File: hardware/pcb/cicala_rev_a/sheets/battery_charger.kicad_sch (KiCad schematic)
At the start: 35 parts, among them J1 USB-C receptacle, J3 Protected LiPo + NTC, U2 BQ25185DLH, U3 TPS63802DLA, U4 USBLC6-2SC6, U5 TPS22917DBVR

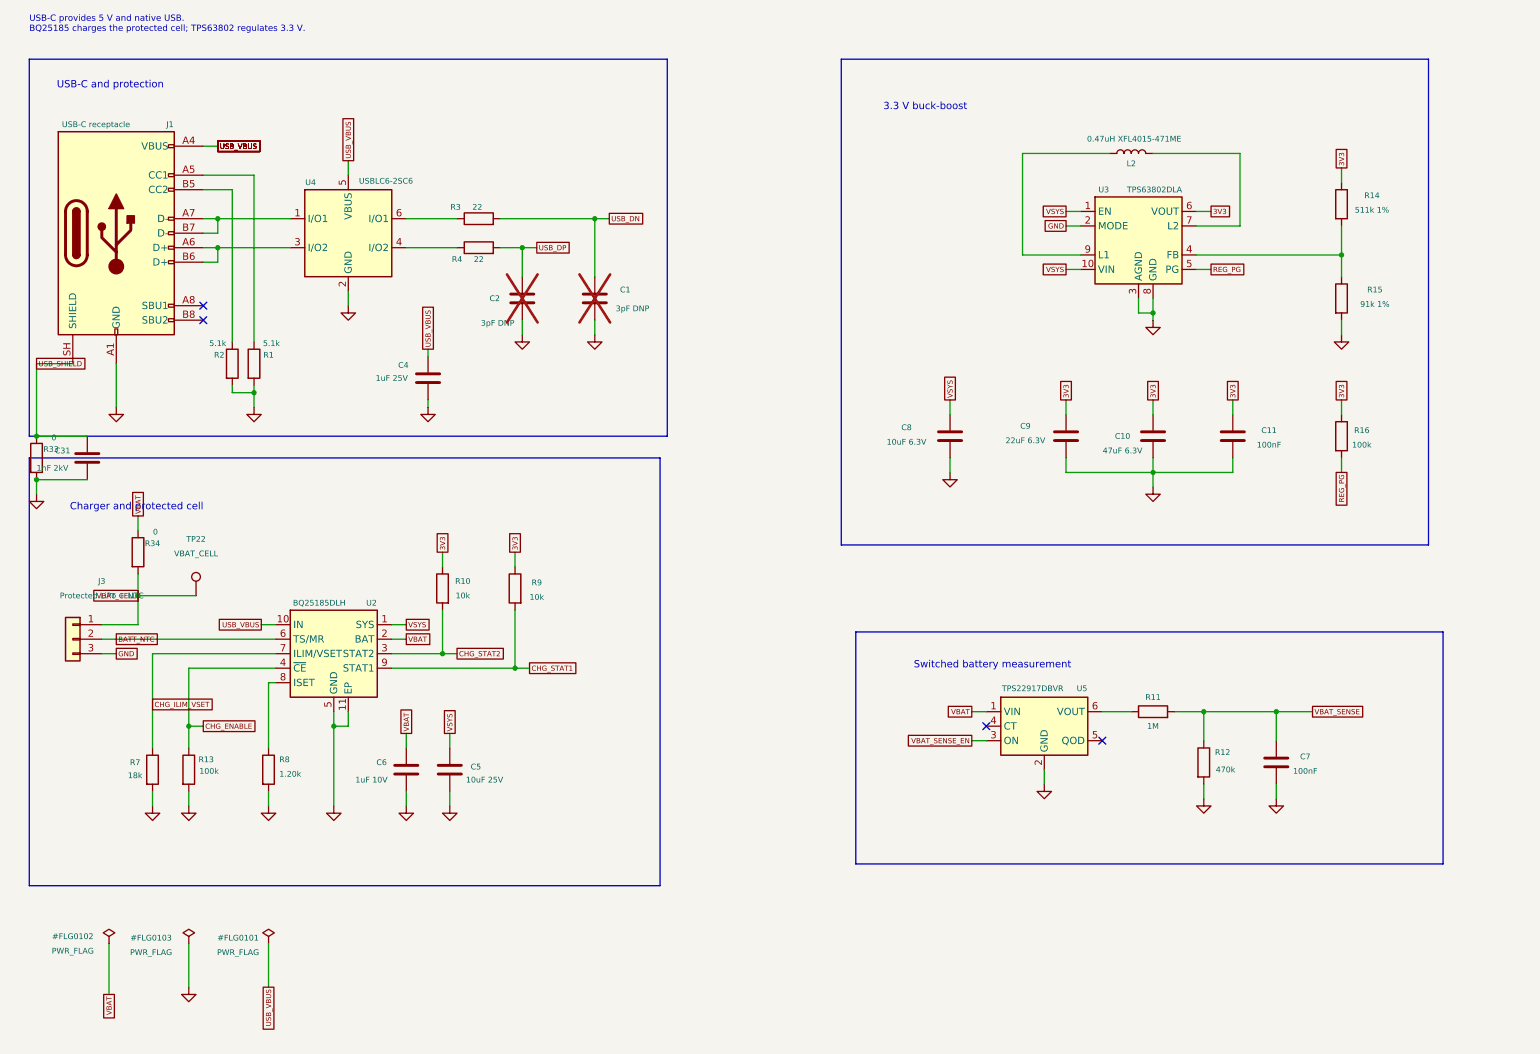
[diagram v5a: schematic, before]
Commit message: refactor(hw): make the root sheet a real hierarchy
The root was three boxes and a filename; every cross-sheet signal travelled
by global label, so nothing recorded which block produced a signal and which
consumed it. The 19 nets that actually cross a sheet boundary are now
hierarchical: each child carries a directional hierarchical label and the
root carries the matching sheet pin, wired block to block. The root also
states the power flow in words.

GND stays global; a ground symbol reads better than a pin on every block.
Root-level global labels keep the plain net names that pin_contract.csv and
the firmware refer to, rather than the sheet-path names a local label gives.

Connectivity is unchanged: the exported netlist is identical to the one
before the conversion, net for net and pin for pin.

Also hides the PWR_FLAG references, moves the USB shield network and the
cell-current link inside the blocks they belong to, and gives every page the
same company, revision and date.

Co-Authored-By: Claude Opus 5 <noreply@anthropic.com>
Claude-Session: https://claude.ai/code/session_01E5vy1HJsPztSk9nFw6j5Ko
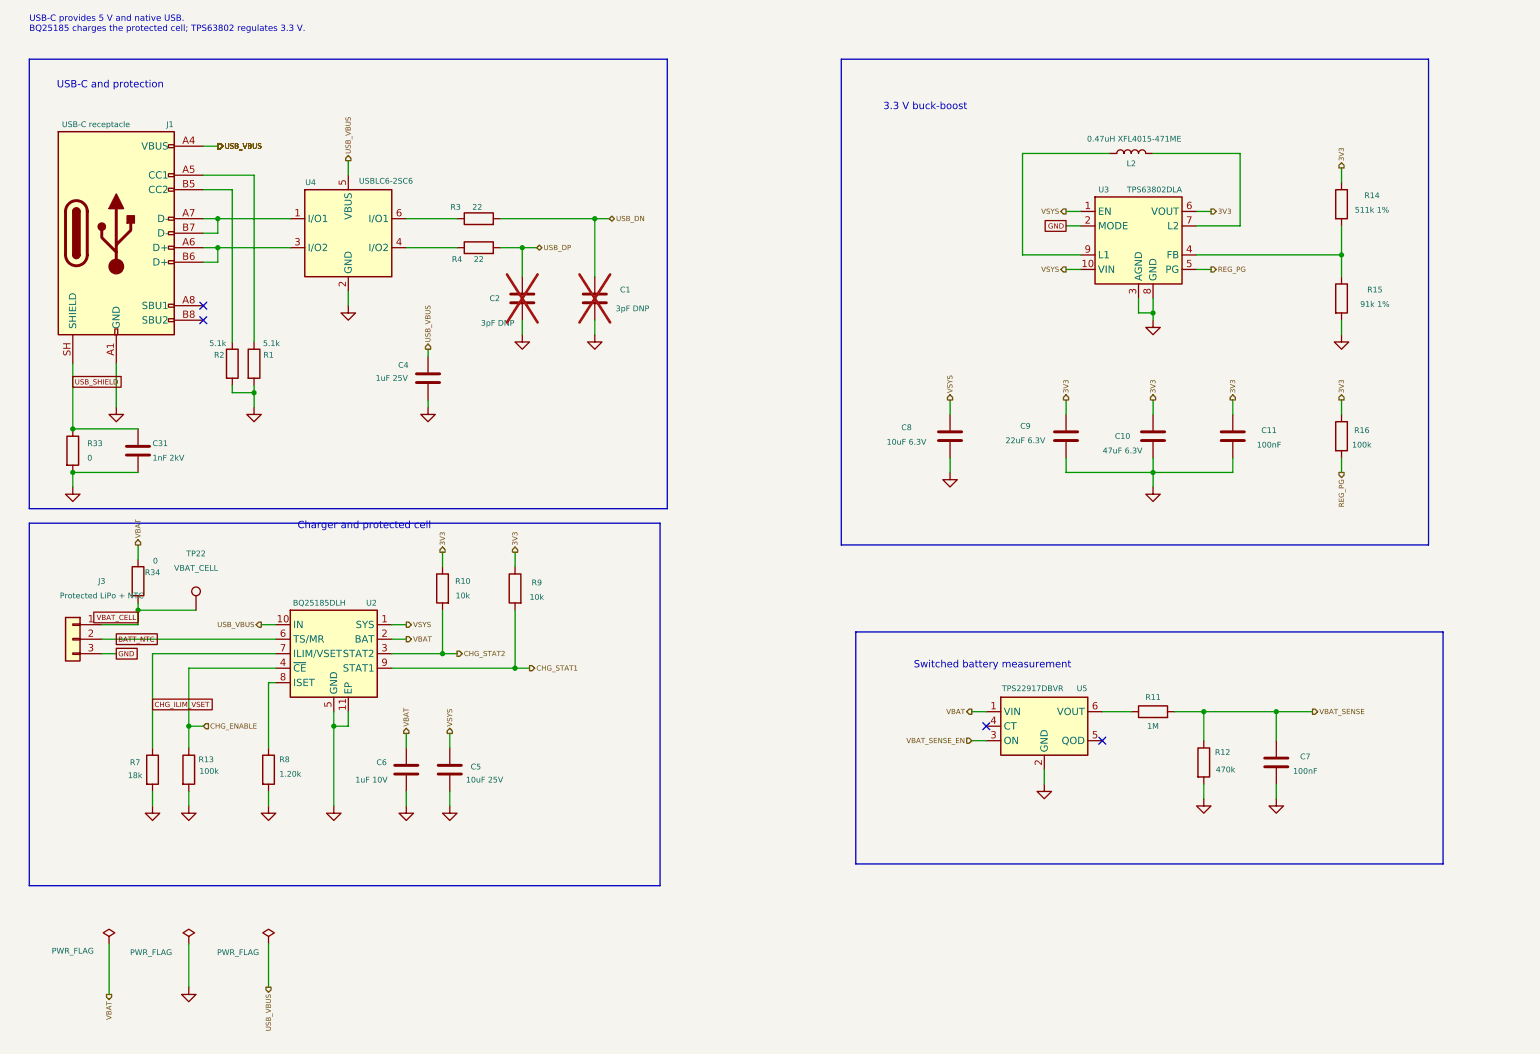
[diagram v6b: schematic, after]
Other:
- company: (none) -> Cicala
- moved on the sheet: C31, R33, R34, TP22

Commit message: feat(hw): place the Rev A board
Everything except the two switches and the display stack sits on the
underside, in the cell cavity, because the sloped roof leaves 0.8 to 3.5 mm
above the board. The module goes rear-left with its antenna at the board
edge and clear of the display; the cell keep-out, the power block and the
front connector row follow from that.

Placement is generated rather than dragged, so it can be regenerated after a
schematic change: anchors are chosen by hand, the rest are packed into free
regions ordered by distance to the pads they already share a net with.

Board is 78 x 49 mm at (3, 3.5). It grew 4 mm deeper than the old 78 x 45
because a USB-C plug could never have reached a receptacle sitting 6 mm
behind the case wall; the front edge now ends 1.5 mm from it and the
receptacle noses into the wall aperture.

Mounting holes become NPTH footprints instead of circles on Edge.Cuts, so
they are drilled rather than routed, and they move to x=13 to clear
Espressif's antenna keep-out, which the module footprint carries and which
reaches 9.5 mm in from the left edge.

J1 gets a project footprint whose silkscreen stops at the board edge; the
library outline would print past it, because the part deliberately overhangs.

Netclasses: Power 0.4 mm, USB 0.29 mm at a 0.29 mm gap for 90 ohm
differential over the declared 0.18 mm prepreg, HV 0.2 mm, which is the gap
the panel's own 0.5 mm-pitch connector allows.

DRC reports zero violations and zero schematic-parity issues. The 216
unconnected items are the routing, which is the next commit.

Co-Authored-By: Claude Opus 5 <noreply@anthropic.com>
Claude-Session: https://claude.ai/code/session_01E5vy1HJsPztSk9nFw6j5Ko
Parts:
- J1: footprint Connector_USB:USB_C_Receptacle_HRO_TYPE-C-31-M-12 -> cicala:USB_C_Receptacle_HRO_TYPE-C-31-M-12_EdgeOverhang
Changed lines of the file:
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@@
 			)
 		)
-		(property "Footprint" "Connector_USB:USB_C_Receptacle_HRO_TYPE-C-31-M-12"
+		(property "Footprint" "cicala:USB_C_Receptacle_HRO_TYPE-C-31-M-12_EdgeOverhang"
 			(at 29.21 53.34 0)
 			(hide yes)
